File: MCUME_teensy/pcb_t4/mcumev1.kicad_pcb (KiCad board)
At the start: 2 copper layers, 72.4 x 101.6 mm, 0 parts

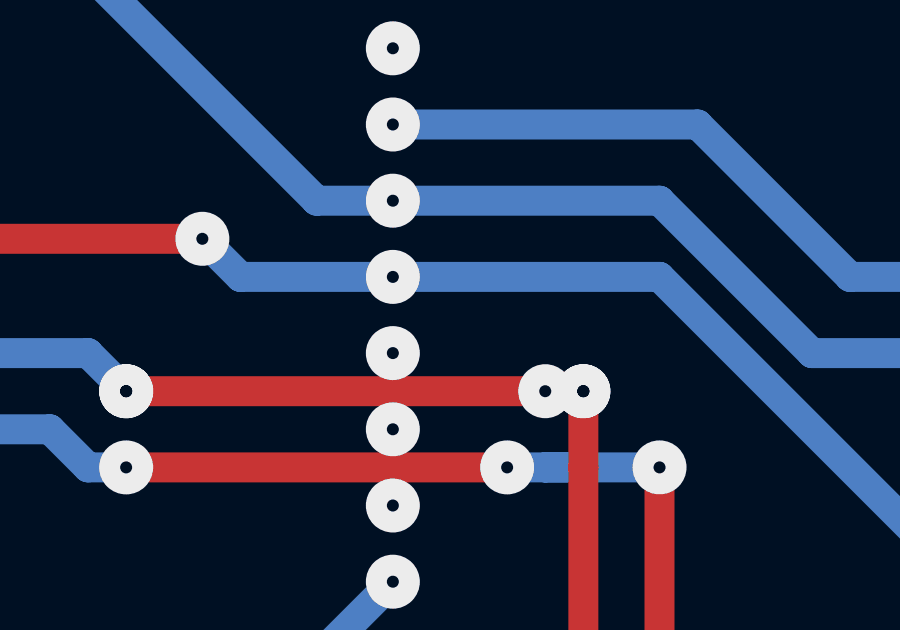
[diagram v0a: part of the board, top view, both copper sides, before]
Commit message: add support for 320x240 st7789 display
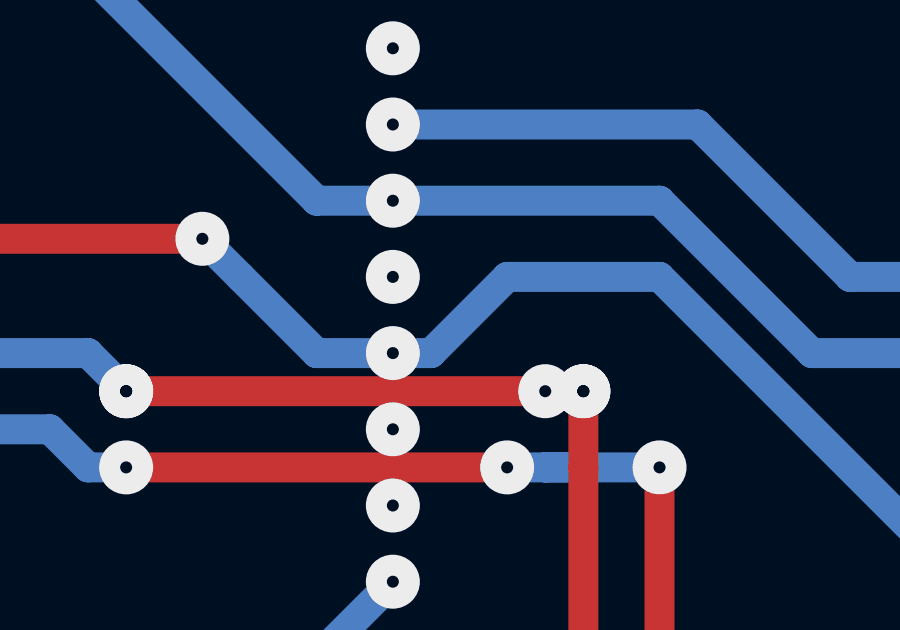
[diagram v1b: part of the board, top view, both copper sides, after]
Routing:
- net (no net): track 1288.6 -> 1290.7 mm
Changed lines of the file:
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@@
     (thickness 1.6)
     (drawings 4)
-    (tracks 386)
+    (tracks 389)
     (zones 0)
     (modules 0)
@@
   (via (at 57.15 22.86) (size 1.8) (drill 0.4) (layers F.Cu B.Cu) (net 0))
   (segment (start 50.8 26.67) (end 54.61 26.67) (width 1) (layer B.Cu) (net 0))
-  (segment (start 74.93 24.13) (end 69.85 24.13) (width 1) (layer B.Cu) (net 0))
   (segment (start 54.61 26.67) (end 55.88 25.4) (width 1) (layer B.Cu) (net 0))
   (segment (start 50.8 21.59) (end 48.26 21.59) (width 1) (layer B.Cu) (net 0))
@@
   (segment (start 93.98 34.29) (end 101.6 34.29) (width 1) (layer B.Cu) (net 0))
   (segment (start 83.82 24.13) (end 93.98 34.29) (width 1) (layer B.Cu) (net 0))
-  (segment (start 74.93 24.13) (end 83.82 24.13) (width 1) (layer B.Cu) (net 0))
   (segment (start 95.25 43.18) (end 93.98 43.18) (width 1) (layer B.Cu) (net 0))
   (segment (start 93.98 43.18) (end 91.44 43.18) (width 1) (layer B.Cu) (net 0))
@@
   (segment (start 110.49 81.28) (end 110.49 26.67) (width 1) (layer B.Cu) (net 0))
   (segment (start 110.49 81.28) (end 110.49 95.25) (width 1) (layer F.Cu) (net 0))
+  (segment (start 69.85 24.13) (end 72.39 26.67) (width 1) (layer B.Cu) (net 0))
+  (segment (start 72.39 26.67) (end 74.93 26.67) (width 1) (layer B.Cu) (net 0))
+  (segment (start 78.742792 24.13) (end 83.82 24.13) (width 1) (layer B.Cu) (net 0))
+  (segment (start 76.202792 26.67) (end 78.742792 24.13) (width 1) (layer B.Cu) (net 0))
+  (segment (start 74.93 26.67) (end 76.202792 26.67) (width 1) (layer B.Cu) (net 0))
 )
